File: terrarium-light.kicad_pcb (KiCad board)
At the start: 2 copper layers, 100 x 100 mm, 2 parts, among them Q1 UMH3N, U1 CH340C

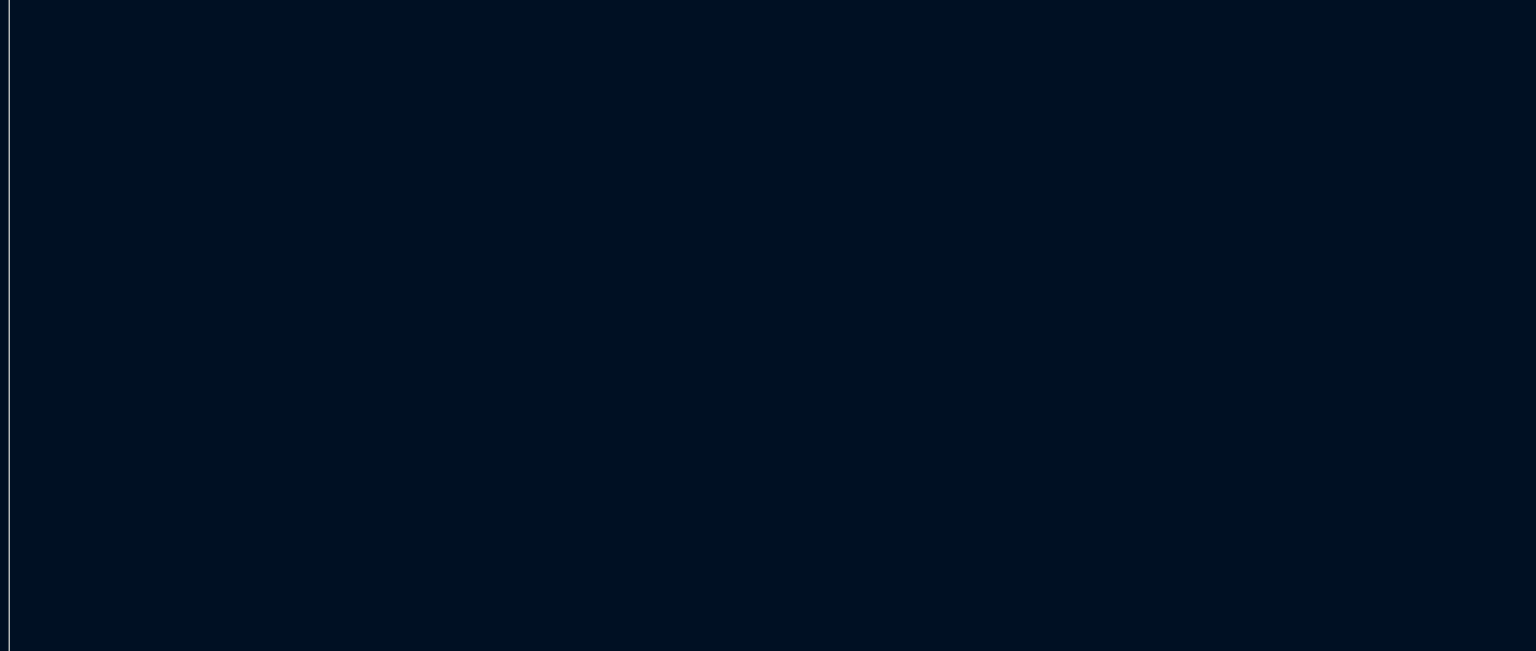
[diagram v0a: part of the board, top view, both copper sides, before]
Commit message: what
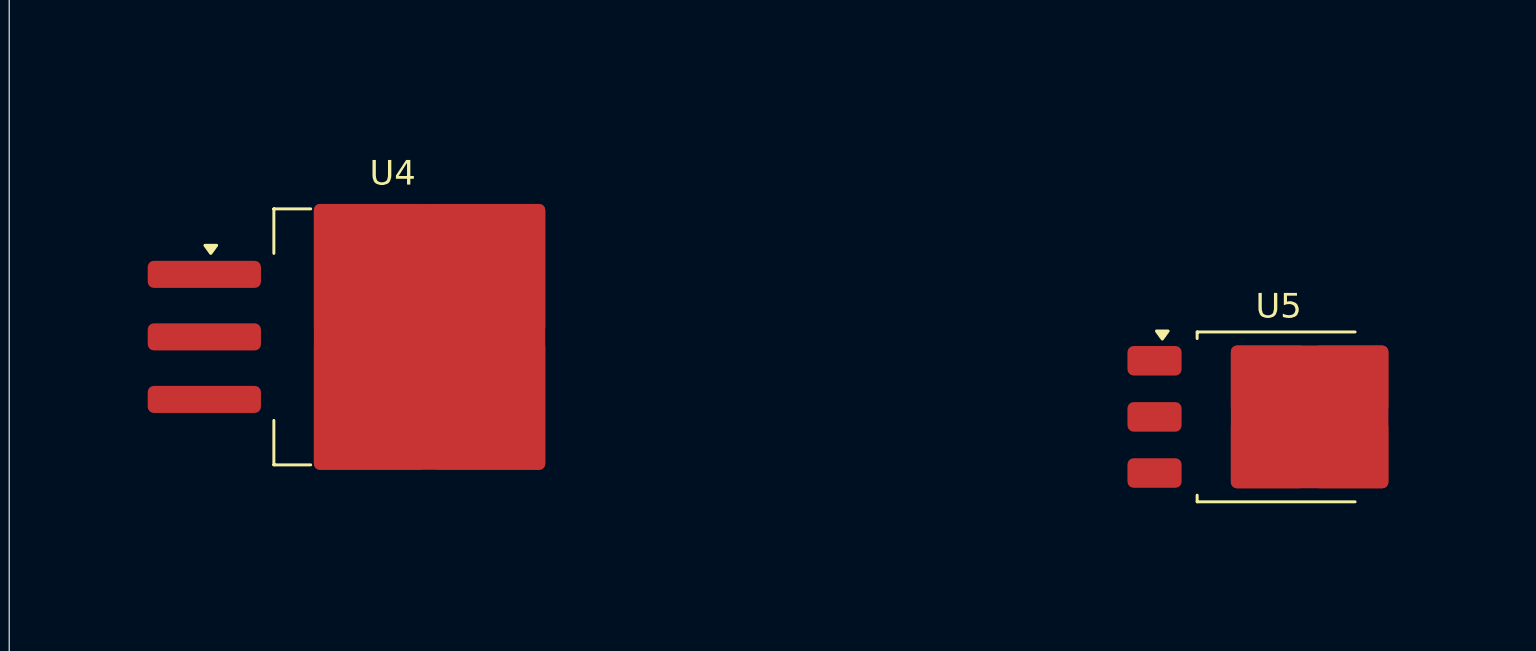
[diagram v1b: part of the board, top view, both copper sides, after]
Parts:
- added U4: LM1117S-3.3, Package_TO_SOT_SMD:TO-263-3_TabPin2, F.Cu at (40.6, 39.2)
- added U5: LM1117DT-3.3, Package_TO_SOT_SMD:TO-252-3_TabPin2, F.Cu at (76.6, 42.5)
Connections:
- net /IO0 renamed /ESP_IO0
- Q1 pad 6: /~{RTS} -> /ESP_EN
- U1 pad 16: unconnected-(U1-VCC-Pad16) -> +3.3V
- U1 pad 4: unconnected-(U1-V3-Pad4) -> +3.3V

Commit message: added footprint
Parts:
- added D1: LED, LED_SMD:LED_SPMWHD32AMH0XAR0PR, F.Cu at (32.0, 56.5)
- added D10: LED, LED_SMD:LED_SPMWHD32AMH0XAR0PR, F.Cu at (66.4, 76.5)
- added D11: LED, LED_SMD:LED_SPMWHD32AMH0XAR0PR, F.Cu at (49.2, 76.5)
- added D12: LED, LED_SMD:LED_SPMWHD32AMH0XAR0PR, F.Cu at (32.0, 76.5)
- added D15: LED, LED_SMD:LED_SPMWHD32AMH0XAR0PR, F.Cu at (32.0, 96.5)
- added D16: LED, LED_SMD:LED_SPMWHD32AMH0XAR0PR, F.Cu at (49.2, 96.5)
- added D17: LED, LED_SMD:LED_SPMWHD32AMH0XAR0PR, F.Cu at (66.4, 96.5)
- added D18: LED, LED_SMD:LED_SPMWHD32AMH0XAR0PR, F.Cu at (83.6, 96.5)
- added D19: LED, LED_SMD:LED_SPMWHD32AMH0XAR0PR, F.Cu at (100.8, 96.5)
- added D2: LED, LED_SMD:LED_SPMWHD32AMH0XAR0PR, F.Cu at (49.2, 56.5)
- added D20: LED, LED_SMD:LED_SPMWHD32AMH0XAR0PR, F.Cu at (118.0, 96.5)
- added D21: LED, LED_SMD:LED_SPMWHD32AMH0XAR0PR, F.Cu at (118.0, 116.5)
- added D22: LED, LED_SMD:LED_SPMWHD32AMH0XAR0PR, F.Cu at (100.8, 116.5)
- added D23: LED, LED_SMD:LED_SPMWHD32AMH0XAR0PR, F.Cu at (83.6, 116.5)
- added D24: LED, LED_SMD:LED_SPMWHD32AMH0XAR0PR, F.Cu at (66.4, 116.5)
- added D25: LED, LED_SMD:LED_SPMWHD32AMH0XAR0PR, F.Cu at (49.2, 116.5)
- added D26: LED, LED_SMD:LED_SPMWHD32AMH0XAR0PR, F.Cu at (32.0, 116.5)
- added D3: LED, LED_SMD:LED_SPMWHD32AMH0XAR0PR, F.Cu at (66.4, 56.5)
- added D4: LED, LED_SMD:LED_SPMWHD32AMH0XAR0PR, F.Cu at (83.6, 56.5)
- added D5: LED, LED_SMD:LED_SPMWHD32AMH0XAR0PR, F.Cu at (100.8, 56.5)
- added D6: LED, LED_SMD:LED_SPMWHD32AMH0XAR0PR, F.Cu at (118.0, 56.5)
- added D7: LED, LED_SMD:LED_SPMWHD32AMH0XAR0PR, F.Cu at (118.0, 76.5)
- added D8: LED, LED_SMD:LED_SPMWHD32AMH0XAR0PR, F.Cu at (100.8, 76.5)
- added D9: LED, LED_SMD:LED_SPMWHD32AMH0XAR0PR, F.Cu at (83.6, 76.5)
- added J1: USB_C_Receptacle_USB2.0_14P, Connector_USB:USB_C_Receptacle_GCT_USB4105-xx-A_16P_TopMnt_Horizontal, F.Cu at (35.2, 34.3)
- U5: value LM1117DT-3.3 -> ESP32-S3-MINI-1U; footprint Package_TO_SOT_SMD:TO-252-3_TabPin2 -> RF_Module:ESP32-S2-MINI-1U
- moved Q1 50.1 mm to (93.5, 39.2)
- moved U1 44.5 mm to (84.0, 40.1)
- moved U5 35.3 mm to (111.8, 42.4)
- moved U4 21.0 mm to (61.5, 40.5), turned to 180 degrees
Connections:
- U4 pad 1: unconnected-(U4-GND-Pad1) -> Earth
- U4 pad 2: unconnected-(U4-VO-Pad2) -> +3.3V
- U4 pad 3: unconnected-(U4-VI-Pad3) -> +5V
- U5 pad 1: unconnected-(U5-GND-Pad1) -> Net-(U5-GND-Pad1)
- U5 pad 2: unconnected-(U5-VO-Pad2) -> Net-(U5-GND-Pad1)

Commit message: tried to add some stuff
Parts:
- added U2: TPS61169DCKR, ul_TPS61169DCKR:DCK0005A_N, F.Cu at (39.9, 67.4)
- added U3: TPS61169DCKR, ul_TPS61169DCKR:DCK0005A_N, F.Cu at (39.9, 107.7)
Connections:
- U1 pad 2: unconnected-(U1-TXD-Pad2) -> /ESP_32_RX
- U1 pad 3: unconnected-(U1-RXD-Pad3) -> /ESP_32_TX
- U5 pad 1: Net-(U5-GND-Pad1) -> GND
- U5 pad 2: Net-(U5-GND-Pad1) -> GND
- U5 pad 3: unconnected-(U5-3V3-Pad3) -> +3.3V
- U5 pad 39: unconnected-(U5-TXD0-Pad39) -> /ESP_32_TX
- U5 pad 4: unconnected-(U5-IO0-Pad4) -> /ESP_IO0
- U5 pad 40: unconnected-(U5-RXD0-Pad40) -> /ESP_32_RX
- U5 pad 42: Net-(U5-GND-Pad1) -> GND
- U5 pad 43: Net-(U5-GND-Pad1) -> GND
- U5 pad 45: unconnected-(U5-EN-Pad45) -> /ESP_EN
- U5 pad 46: Net-(U5-GND-Pad1) -> GND
- U5 pad 47: Net-(U5-GND-Pad1) -> GND
- U5 pad 48: Net-(U5-GND-Pad1) -> GND
- U5 pad 49: Net-(U5-GND-Pad1) -> GND
- U5 pad 50: Net-(U5-GND-Pad1) -> GND
- U5 pad 51: Net-(U5-GND-Pad1) -> GND
- U5 pad 52: Net-(U5-GND-Pad1) -> GND
- U5 pad 53: Net-(U5-GND-Pad1) -> GND
- U5 pad 54: Net-(U5-GND-Pad1) -> GND
- U5 pad 55: Net-(U5-GND-Pad1) -> GND
- U5 pad 56: Net-(U5-GND-Pad1) -> GND
- U5 pad 57: Net-(U5-GND-Pad1) -> GND
- U5 pad 58: Net-(U5-GND-Pad1) -> GND
- U5 pad 59: Net-(U5-GND-Pad1) -> GND
- U5 pad 60: Net-(U5-GND-Pad1) -> GND
- U5 pad 61: Net-(U5-GND-Pad1) -> GND
- U5 pad 62: Net-(U5-GND-Pad1) -> GND
- U5 pad 63: Net-(U5-GND-Pad1) -> GND
- U5 pad 64: Net-(U5-GND-Pad1) -> GND
- U5 pad 65: Net-(U5-GND-Pad1) -> GND

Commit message: found more parts and added them
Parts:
- removed J1: USB_C_Receptacle_USB2.0_14P, Connector_USB:USB_C_Receptacle_GCT_USB4105-xx-A_16P_TopMnt_Horizontal
- added C1: 4.7uF, Capacitor_SMD:C_0805_2012Metric_Pad1.18x1.45mm_HandSolder, F.Cu at (36.0, 110.5)
- added C10: 10uf, Capacitor_SMD:C_0805_2012Metric_Pad1.18x1.45mm_HandSolder, F.Cu at (138.0, 45.5)
- added C11: 0.1uf, Capacitor_SMD:C_0805_2012Metric_Pad1.18x1.45mm_HandSolder, F.Cu at (138.0, 48.5)
- added C2: 4.7uF, Capacitor_SMD:C_0805_2012Metric_Pad1.18x1.45mm_HandSolder, F.Cu at (45.5, 110.5)
- added C3: 4.7uF, Capacitor_SMD:C_0805_2012Metric_Pad1.18x1.45mm_HandSolder, F.Cu at (69.5, 68.0)
- added C4: 4.7uF, Capacitor_SMD:C_0805_2012Metric_Pad1.18x1.45mm_HandSolder, F.Cu at (38.0, 75.0)
- added C5: 0.1uF, Capacitor_SMD:C_0805_2012Metric_Pad1.18x1.45mm_HandSolder, F.Cu at (138.0, 30.4)
- added C6: 0.1uF, Capacitor_SMD:C_0805_2012Metric_Pad1.18x1.45mm_HandSolder, F.Cu at (138.0, 33.5)
- added C7: 1uF, Capacitor_SMD:C_0805_2012Metric_Pad1.18x1.45mm_HandSolder, F.Cu at (138.0, 36.5)
- added C8: 10uf, Capacitor_SMD:C_0805_2012Metric_Pad1.18x1.45mm_HandSolder, F.Cu at (138.0, 39.5)
- added C9: 22uF, Capacitor_SMD:C_0805_2012Metric_Pad1.18x1.45mm_HandSolder, F.Cu at (138.0, 42.5)
- added D13: SK16, Diode_SMD:D_SMA_Handsoldering, F.Cu at (34.5, 67.0)
- added D14: SK16, Diode_SMD:D_SMA_Handsoldering, F.Cu at (49.5, 105.0)
- added J2: USB_C_Receptacle_USB2.0_16P, Connector_USB:USB_C_Receptacle_HCTL_HC-TYPE-C-16P-01A, F.Cu at (34.6, 33.4)
- added L1: VLS6045EX-100M-H, Inductor_SMD:L_TDK_VLS6045EX_VLS6045AF, F.Cu at (57.5, 67.0)
- added L2: VLS6045EX-100M-H, Inductor_SMD:L_TDK_VLS6045EX_VLS6045AF, F.Cu at (41.0, 103.5)
- added R1: 2.04ohm, Resistor_SMD:R_0805_2012Metric_Pad1.20x1.40mm_HandSolder, F.Cu at (41.0, 62.0)
- added R2: 2.04ohm, Resistor_SMD:R_0805_2012Metric_Pad1.20x1.40mm_HandSolder, F.Cu at (31.5, 110.5)
- added R3: 5.1K, Resistor_SMD:R_0805_2012Metric_Pad1.20x1.40mm_HandSolder, F.Cu at (142.7, 30.4)
- added R4: 5.1K, Resistor_SMD:R_0805_2012Metric_Pad1.20x1.40mm_HandSolder, F.Cu at (142.7, 33.4)
- U2, U3: footprint ul_TPS61169DCKR:DCK0005A_N -> Package_TO_SOT_SMD:SOT-353_SC-70-5_Handsoldering
- moved U2 4.63 mm to (44.5, 67.5)
- moved U3 3.48 mm to (40.8, 111.0)
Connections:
- U2 pad 2: Earth -> GND
- U3 pad 2: Earth -> GND
- U4 pad 1: Earth -> GND

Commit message: more stuff
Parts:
- removed U5: ESP32-S3-MINI-1U, RF_Module:ESP32-S2-MINI-1U
- added FB1: MI0805K400R-10, Resistor_SMD:R_0805_2012Metric_Pad1.20x1.40mm_HandSolder, F.Cu at (85.0, 60.0)
- added U6: ESP32-S3-MINI-1, RF_Module:ESP32-S2-MINI-1, F.Cu at (100.0, 139.2)
- moved R2 117.1 mm to (144.0, 78.0), turned to 90 degrees
- moved D26 115.8 mm to (143.0, 83.5)
- moved C1 115.4 mm to (143.0, 67.5)
- moved L2 103.2 mm to (137.0, 65.5), turned to 180 degrees
- moved U3 102.5 mm to (136.8, 75.0), turned to 90 degrees
- moved D6 98.4 mm to (72.0, 143.5)
- moved D15 96.9 mm to (128.0, 83.5)
- moved D25 96.1 mm to (143.0, 95.5)
- moved C5 91.5 mm to (97.5, 112.5), turned to -90 degrees
- moved D7 90.6 mm to (57.0, 143.5)
- moved D14 83.9 mm to (128.0, 75.5), turned to 90 degrees
- moved C2 83.6 mm to (123.0, 79.0), turned to 180 degrees
- moved D5 80.3 mm to (72.0, 131.5)
- moved C6 79.6 mm to (93.5, 99.5), turned to -90 degrees
- moved D16 78.8 mm to (128.0, 95.5)
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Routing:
- net +5V: track 0.00 -> 48.0 mm
- net Net-(D13-A): track 0.00 -> 21.7 mm
- net Net-(D12-K): track 0.00 -> 16.4 mm
- net Net-(D20-K): track 0.00 -> 15.9 mm
- net VBUS: track 0.00 -> 14.4 mm
- net Net-(D14-A): track 0.00 -> 10.4 mm
- net Net-(D8-K): track 0.00 -> 9.75 mm
- net Net-(D7-K): track 0.00 -> 9.75 mm
- net Net-(D25-K): track 0.00 -> 9.75 mm
- net Net-(D24-K): track 0.00 -> 9.75 mm
- net Net-(D23-K): track 0.00 -> 9.75 mm
- net Net-(D22-K): track 0.00 -> 9.75 mm
- net Net-(D21-K): track 0.00 -> 9.75 mm
- net Net-(D11-K): track 0.00 -> 9.75 mm
- net Net-(D10-K): track 0.00 -> 9.75 mm
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
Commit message: big redo
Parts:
- moved FB1 121.7 mm to (206.5, 66.5), turned to 0 degrees
- moved U6 114.4 mm to (45.6, 38.5), turned to 90 degrees
- moved C11 107.7 mm to (188.0, 69.7), turned to 0 degrees
- moved R4 105.8 mm to (200.5, 81.8), turned to 0 degrees
- moved C10 99.4 mm to (188.0, 66.7), turned to 0 degrees
- moved R3 99.4 mm to (202.0, 75.0)
- moved D14 97.3 mm to (212.1, 26.7), turned to 0 degrees
- moved C5 95.8 mm to (183.2, 69.7), turned to 0 degrees
- moved C8 93.8 mm to (188.0, 60.7), turned to 0 degrees
- moved C6 93.6 mm to (183.2, 72.7), turned to 0 degrees
- moved C7 91.0 mm to (193.5, 56.5)
- moved C9 87.0 mm to (188.0, 63.7)
- moved U3 83.4 mm to (210.0, 34.9), turned to 0 degrees
- moved D17 70.3 mm to (189.0, 142.5)
- moved D18 70.0 mm to (188.0, 155.5)
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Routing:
- net +5V: track 48.0 -> 9.63 mm
- net Net-(D20-K): track 15.9 -> 0.00 mm
- net Net-(D12-K): track 16.4 -> 1.90 mm
- net VBUS: track 14.4 -> 0.00 mm
- net Net-(D14-A): track 10.4 -> 0.00 mm
- net Net-(D8-K): track 9.75 -> 0.00 mm
- net Net-(D7-K): track 9.75 -> 0.00 mm
- net Net-(D25-K): track 9.75 -> 0.00 mm
- net Net-(D24-K): track 9.75 -> 0.00 mm
- net Net-(D23-K): track 9.75 -> 0.00 mm
- net Net-(D22-K): track 9.75 -> 0.00 mm
- net Net-(D21-K): track 9.75 -> 0.00 mm
- net Net-(D11-K): track 9.75 -> 0.00 mm
- net Net-(D10-K): track 9.75 -> 0.00 mm
- net Net-(D10-A): track 9.75 -> 0.00 mm
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
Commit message: better layout
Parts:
- moved D14 104.6 mm to (124.0, 83.0), turned to 90 degrees
- moved U3 94.2 mm to (129.0, 83.0)
- moved R2 82.9 mm to (128.0, 87.0), turned to -90 degrees
- moved D16 73.4 mm to (118.5, 107.0)
- moved D17 73.4 mm to (120.0, 117.5)
- moved D18 73.4 mm to (119.0, 130.5)
- moved D15 72.4 mm to (119.0, 96.5)
- moved L2 64.3 mm to (130.0, 78.0), turned to 180 degrees
- moved D19 61.1 mm to (119.0, 142.0)
- moved C2 57.3 mm to (123.0, 89.0), turned to 180 degrees
- moved D25 54.0 mm to (144.0, 100.1)
- moved D20 50.7 mm to (133.0, 122.1)
- moved C1 47.5 mm to (134.0, 83.0)
- moved D24 37.6 mm to (144.0, 110.1)
- moved D21 35.0 mm to (143.0, 141.5)
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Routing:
- net Net-(D13-A): track 12.5 -> 0.00 mm
- net +5V: track 9.63 -> 0.00 mm
- net Net-(D1-A): track 3.71 -> 0.00 mm
- net GND: track 2.50 -> 0.00 mm
- net Net-(D12-K): track 1.90 -> 0.00 mm
